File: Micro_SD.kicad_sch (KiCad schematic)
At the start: 3 parts, among them J2 DM3BT-DSF-PEJS

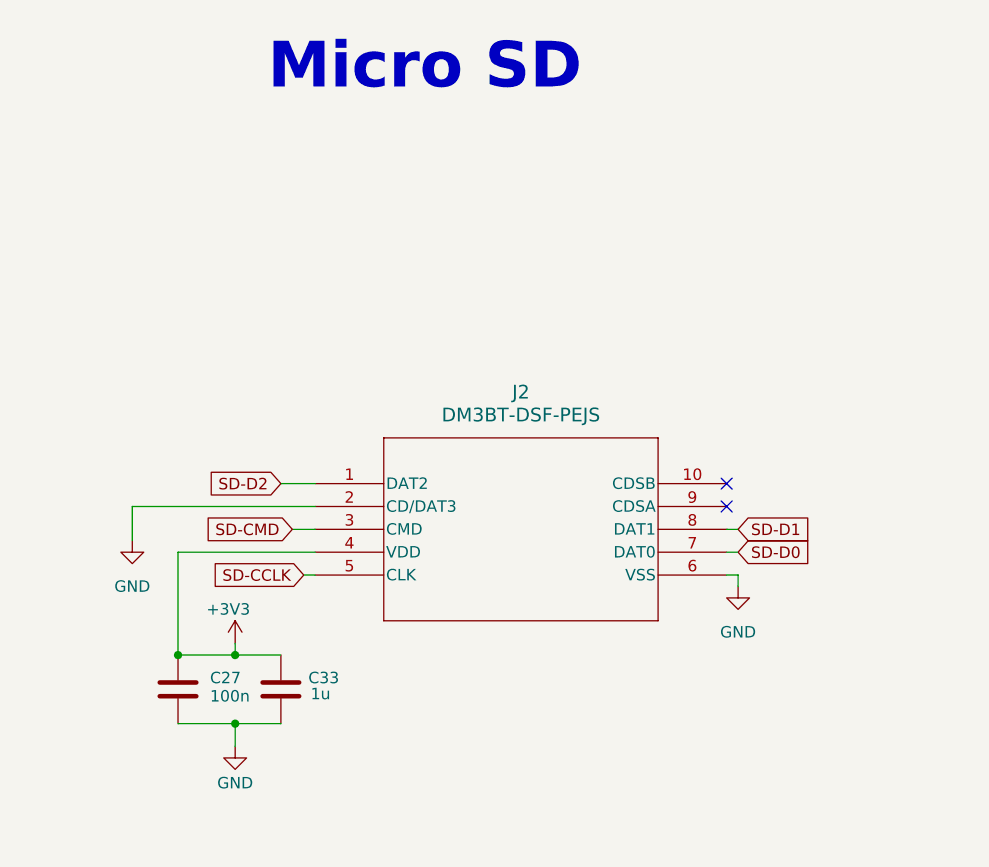
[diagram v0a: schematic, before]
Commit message: Fixed GND issues with connector and mounting holes
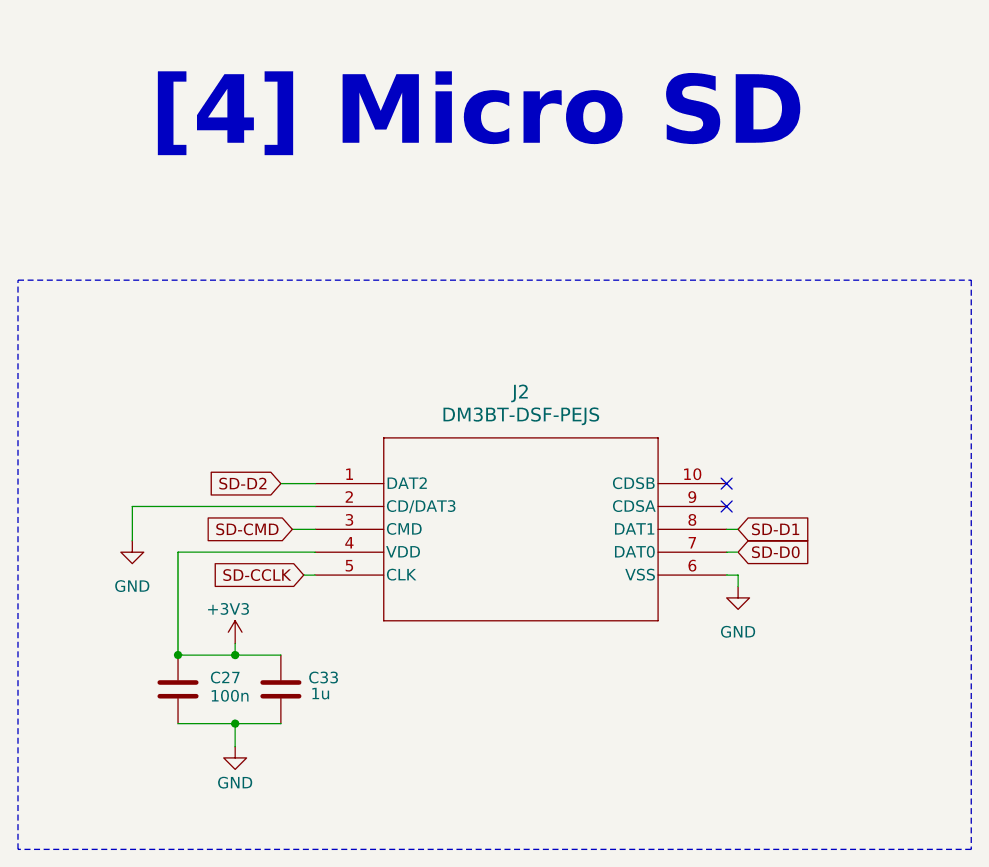
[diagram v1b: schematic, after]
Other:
- note added: "[4] Micro SD"
- note removed: "Micro SD"
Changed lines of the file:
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@@
 	(generator_version "9.0")
 	(paper "A4")
-	(text "Micro SD"
+	(rectangle
+		(start 95.25 47.244)
+		(end 201.168 110.49)
+		(stroke
+			(width 0)
+			(type dash)
+		)
+		(fill
+			(type none)
+		)
+	)
+	(text "[4] Micro SD"
 		(exclude_from_sim no)
-		(at 140.462 23.622 0)
+		(at 146.304 28.702 0)
 		(effects
 			(font
-				(size 5.08 5.08)
-				(thickness 0.508)
+				(size 7.62 7.62)
+				(thickness 1.524)
 				(bold yes)
 			)
